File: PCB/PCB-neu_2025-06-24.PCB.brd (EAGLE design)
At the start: 60 x 60 mm, 16 parts

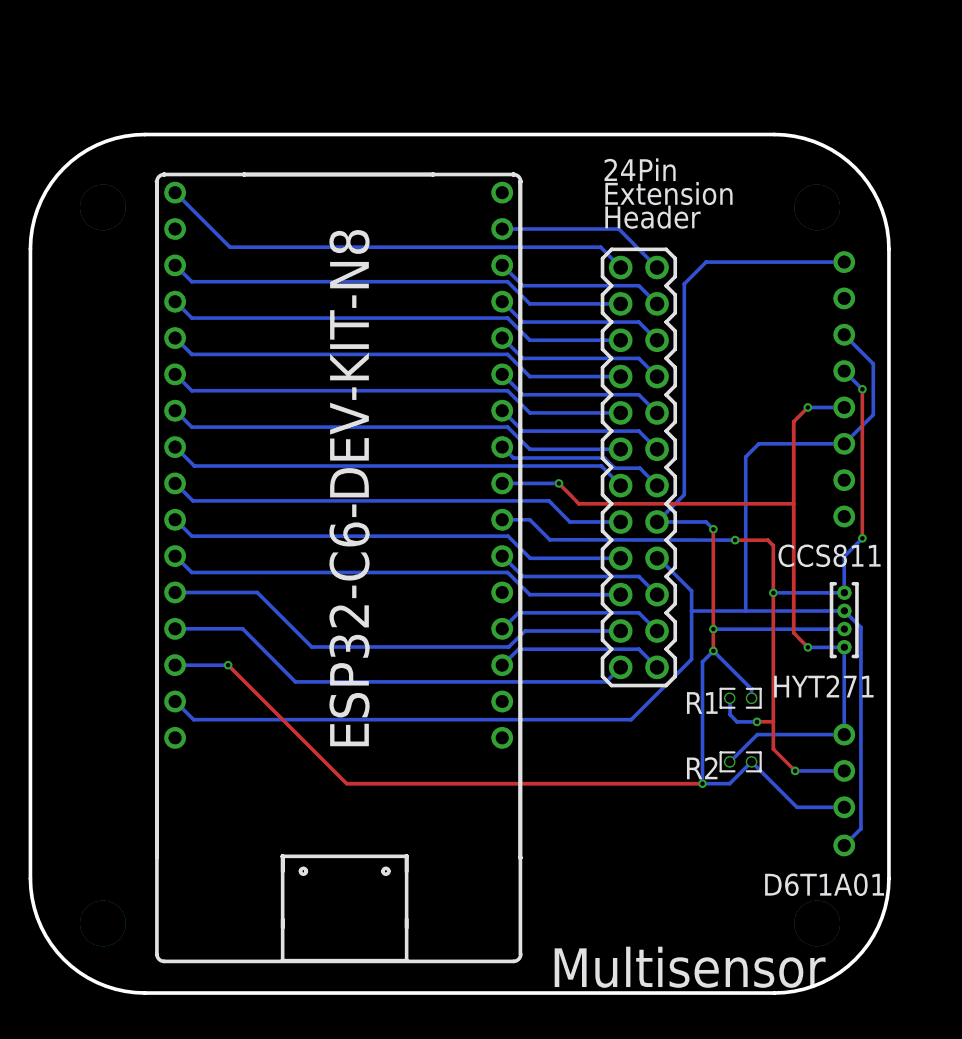
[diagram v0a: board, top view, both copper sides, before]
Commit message: PCB Update Lochdurchmesser auf 0,6+
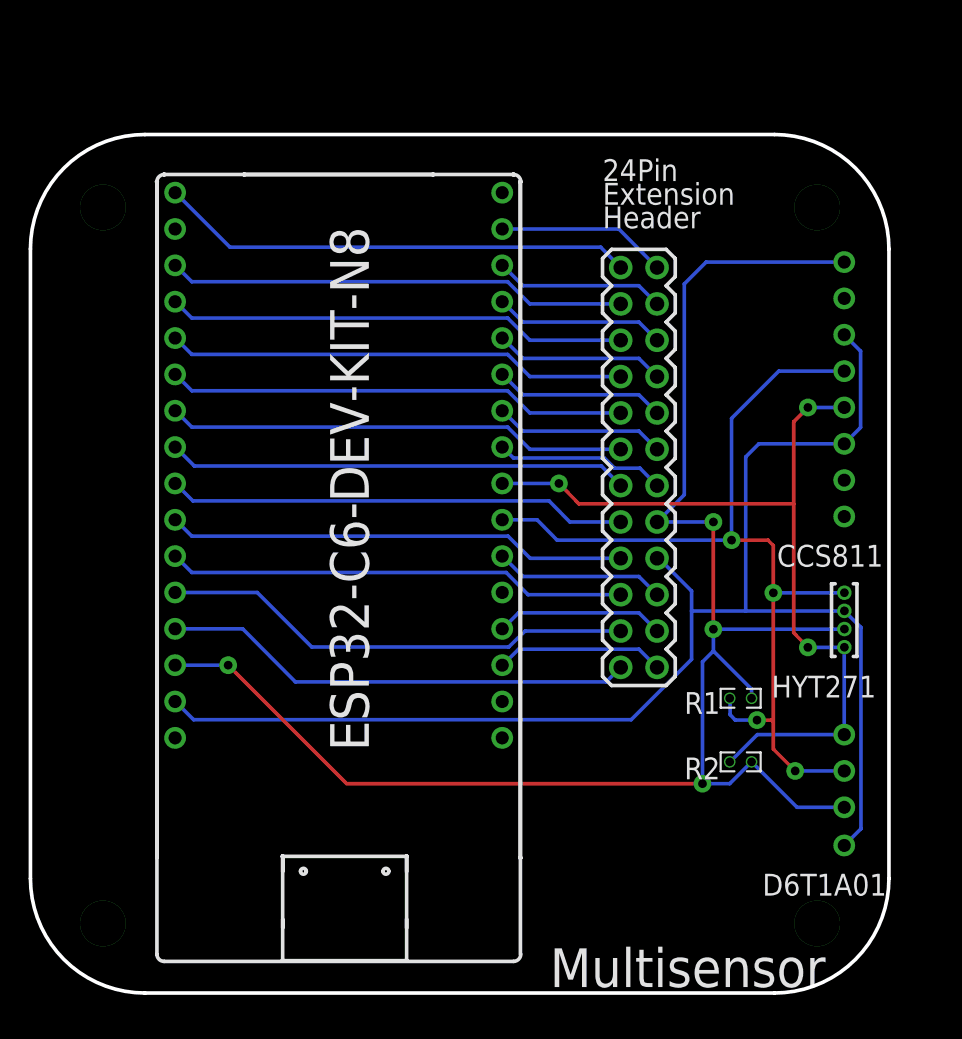
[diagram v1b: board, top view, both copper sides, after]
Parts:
- removed WAAYAVHK: (no value), PCB-neu_2025-06-15:WAAYAVHK_1PRIMARY
- added CONAYFJX: (no value), PCB-neu_2025-06-24:CONAYFJX_1PRIMARY
- 24: device PCB-neu_2025-06-15:PIN-HEADER-210S-2X12P_WK_1PRIMARY -> PCB-neu_2025-06-24:PIN-HEADER-210S-2X12P_WK_1PRIMARY
- CCS811: device PCB-neu_2025-06-15:CCS811_JOY-IT_1PRIMARY -> PCB-neu_2025-06-24:CCS811_JOY-IT_1PRIMARY
- D6T1A01: device PCB-neu_2025-06-15:D6T1A01_1PRIMARY -> PCB-neu_2025-06-24:D6T1A01_1PRIMARY
- DUMMY1, DUMMY2, DUMMY3, DUMMY4: device PCB-neu_2025-06-15:P:EX40Y40D201 -> PCB-neu_2025-06-24:P:EX40Y40D241
- DUMMY5, DUMMY6, DUMMY7, DUMMY8: device PCB-neu_2025-06-15:P:EX126Y126D1261 -> PCB-neu_2025-06-24:P:EX126Y126D1261
- ESP32-C6-DEVKITC-1: device PCB-neu_2025-06-15:ESP32-C6-DEV-KIT-N8_1PRIMARY -> PCB-neu_2025-06-24:ESP32-C6-DEV-KIT-N8_1PRIMARY
- HYT271: device PCB-neu_2025-06-15:HYT271_1PRIMARY -> PCB-neu_2025-06-24:HYT271_1PRIMARY
- R1, R2: device PCB-neu_2025-06-15:R0603_1PRIMARY -> PCB-neu_2025-06-24:R0603_1PRIMARY
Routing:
- net SDA: track 65.4 -> 66.6 mm, vias 6 -> 4
- net GND: track 101.8 -> 101.1 mm
- net 5V0: track 117.1 -> 116.9 mm, vias 5 -> 4
